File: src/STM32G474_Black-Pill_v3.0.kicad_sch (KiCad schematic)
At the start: 0 parts

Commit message: Add: Schematic to the project. Also added some documents.
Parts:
- added C101, C103, C108, C109, C110, C111, C112, C114, C116, C119, C120: 100nF, symbol Device:C
- added C107: 10µF, symbol Device:C
- added C113, C115, C117, C118: 1µF, symbol Device:C
- added C205, C206, C214, C215: 6pF, Capacitor_SMD:C_0402_1005Metric_Pad0.74x0.62mm_HandSolder, symbol Device:C
- added D101: red, symbol Device:LED
- added D102: BAT54C, Package_TO_SOT_SMD:SOT-23, symbol Diode:BAT54C
- added D103: green, symbol Device:LED
- added J101: USB_C_Receptacle_USB2.0, symbol Connector:USB_C_Receptacle_USB2.0
- added J102, J103: Conn_01x20, symbol Connector_Generic:Conn_01x24
- added J104: Conn_01x04, symbol Connector_Generic:Conn_01x04
- added L101: 10µH, symbol Device:L
- added R101, R102: 5.1k, symbol Device:R
- added R103, R108: 10k, symbol Device:R
- added R104, R105: 10R, symbol Device:R
- added R107, R109: 100R, symbol Device:R
- added R218: 0R, Resistor_SMD:R_0603_1608Metric_Pad0.98x0.95mm_HandSolder, symbol Device:R
- added SW101, SW102, SW103: SW_Push, symbol Switch:SW_Push
- added U101: W25Q32JVSS, Package_SO:SOIC-8_5.23x5.23mm_P1.27mm, symbol Memory_Flash:W25Q32JVSS
- added U102: STM32G474RETx, Package_QFP:LQFP-64_10x10mm_P0.5mm, symbol MCU_ST_STM32G4:STM32G474RETx
- added U103: AP7343xx, Package_TO_SOT_SMD:SOT-23-5, symbol Regulator_Linear_User:AP7343xx
- added Y201: 24MHz, Crystal:Crystal_SMD_SeikoEpson_FA128-4Pin_2.0x1.6mm, symbol Device:Crystal_GND24_Small
- added Y202: 32.768kHz, Crystal:Crystal_SMD_MicroCrystal_CC7V-T1A-2Pin_3.2x1.5mm_HandSoldering, symbol Device:Crystal
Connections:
- new net: J101.A6 (D+), J101.B6 (D+), R105.1
- new net: D103.2 (A), R109.2
- new net: C205.2, U102.5 (PF0), Y201.1
- new net: J101.A5 (CC1), R101.1
- new net: J101.A7 (D-), J101.B7 (D-), R104.1
- new net: J101.B5 (CC2), R102.1
- new net: R218.1, U102.6 (PF1)
- new net: C206.2, R218.2, Y201.3
- new net: D101.2 (A), R107.2
- new net +3.3V: C101.1, C107.1, C108.1, C109.1, C110.1, C111.1, C115.1, C116.1, D102.2, J102.20 (Pin_20), J103.3 (Pin_3), J104.1 (Pin_1), L101.1, R103.1, R107.1, R109.1, SW102.2, U101.3 (IO2), U101.7 (IO3), U101.8 (VCC), U102.16 (VDD), U102.32 (VDD), U102.48 (VDD), U102.64 (VDD), U103.5 (OUT)
- new net +5V: C113.1, C114.1, J101.A4 (VBUS), J101.A9 (VBUS), J101.B4 (VBUS), J101.B9 (VBUS), J102.18 (Pin_18), J103.1 (Pin_1), U103.1 (IN), U103.3 (EN)
- new net BOOT: R108.1, SW102.1, U102.61 (PB8)
- new net GND: C101.2, C103.2, C107.2, C108.2, C109.2, C110.2, C111.2, C112.2, C113.2, C114.2, C115.2, C116.2, C117.1, C118.1, C119.1, C120.1, C205.1, C206.1, C214.1, C215.1, D101.1 (K), J101.A1 (GND), J101.A12 (GND), J101.B1 (GND), J101.B12 (GND), J101.S1 (SHIELD), J102.19 (Pin_19), J102.24 (Pin_24), J103.2 (Pin_2), J103.24 (Pin_24), J104.4 (Pin_4), R101.2, R102.2, R108.2, SW101.1, SW103.1, U101.4 (GND), U102.15 (VSS), U102.27 (VSSA), U102.31 (VSS), U102.47 (VSS), U102.63 (VSS), U103.2 (GND), Y201.2, Y201.4
- new net NRST: C103.1, J103.16 (Pin_16), R103.2, SW101.2, U102.7 (PG10)
- new net PA0: J103.4 (Pin_4), U102.12 (PA0)
- new net PA1: J103.5 (Pin_5), U102.13 (PA1)
- new net PA10: J103.14 (Pin_14), U102.44 (PA10)
- new net PA11: R104.2, U102.45 (PA11)
- new net PA12: R105.2, U102.46 (PA12)
- new net PA15: J103.15 (Pin_15), U101.1 (~{CS}), U102.51 (PA15)
- new net PA2: J103.6 (Pin_6), U102.14 (PA2)
- new net PA3: J103.7 (Pin_7), U102.17 (PA3)
- new net PA4: J103.8 (Pin_8), U102.18 (PA4)
- new net PA5: J103.9 (Pin_9), U102.19 (PA5)
- new net PA6: J103.10 (Pin_10), U102.20 (PA6)
- new net PA7: J103.11 (Pin_11), U102.21 (PA7)
- new net PA8: J103.12 (Pin_12), U102.42 (PA8)
- new net PA9: J103.13 (Pin_13), U102.43 (PA9)
- new net PB0: J102.1 (Pin_1), U102.24 (PB0)
- new net PB1: J102.2 (Pin_2), U102.25 (PB1)
- new net PB10: J102.10 (Pin_10), U102.30 (PB10)
- new net PB11: J102.11 (Pin_11), U102.33 (PB11)
- new net PB12: J102.12 (Pin_12), U102.34 (PB12)
- new net PB13: J102.13 (Pin_13), U102.35 (PB13)
- new net PB14: J102.14 (Pin_14), U102.36 (PB14)
- new net PB15: J102.15 (Pin_15), U102.37 (PB15)
- new net PB2: J102.3 (Pin_3), U102.26 (PB2)
- new net PB3: J102.4 (Pin_4), U102.56 (PB3)
- new net PB4: J102.5 (Pin_5), U102.57 (PB4)
- new net PB5: J102.6 (Pin_6), U102.58 (PB5)
- new net PB6: J102.7 (Pin_7), U102.59 (PB6)
- new net PB7: J102.8 (Pin_8), U102.60 (PB7)
- new net PB9: J102.9 (Pin_9), U102.62 (PB9)
- new net PC0: J103.17 (Pin_17), U102.8 (PC0)
- new net PC1: J103.18 (Pin_18), U102.9 (PC1)
- new net PC13: D103.1 (K), J102.23 (Pin_23), U102.2 (PC13)
- new net PC14: C215.2, U102.3 (PC14), Y202.2
- new net PC15: C214.2, U102.4 (PC15), Y202.1
- new net PC2: J103.19 (Pin_19), U102.10 (PC2)
- new net PC3: J103.21 (Pin_21), U102.11 (PC3)
- new net PC4: J103.22 (Pin_22), U102.22 (PC4)
- new net PC5: J103.23 (Pin_23), U102.23 (PC5)
- new net PC6: J102.16 (Pin_16), U102.38 (PC6)
- new net PC7: J102.17 (Pin_17), U102.39 (PC7)
- new net PC8: J102.21 (Pin_21), U102.40 (PC8)
- new net PC9: J102.22 (Pin_22), U102.41 (PC9)
- new net PD2: SW103.2, U102.55 (PD2)
- new net SPI_{3}.MISO: U101.2 (DO(IO1)), U102.53 (PC11)
- new net SPI_{3}.MOSI: U101.5 (DI(IO0)), U102.54 (PC12)
- new net SPI_{3}.SCK: U101.6 (CLK), U102.52 (PC10)
- new net SWCLK: J104.3 (Pin_3), U102.50 (PA14)
- new net SWDIO: J104.2 (Pin_2), U102.49 (PA13)
- new net VB: D102.1, J103.20 (Pin_20)
- new net VBAT: C112.1, D102.3, U102.1 (VBAT)
- new net VREF: C117.2, C118.2, C119.2, C120.2, L101.2, U102.28 (VREF+), U102.29 (VDDA)
- no-connect marks 0 -> 2
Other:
- note added: "3.3V Power Supply"
- note added: "Analog Voltage Supply / Reference"
- note added: "BOOT Button"
- note added: "Battery Voltage"
- note added: "Decoupling Capacitors (MCU)"
- note added: "Flash"
- note added: "HSE"
- note added: "LSE"
- note added: "Pin-Headers"
- note added: "Power LED"
- note added: "Programming"
- note added: "Reset Button"
- note added: "USB-C"
- note added: "User Button"
- note added: "User LED"
- title: <Default Template> -> Black Pill v3.0 (STM32G474)

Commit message: Mod: Schematic, added manufacturer no. and vendor no.
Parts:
- C101, C108, C109, C110, C111, C112, C114, C116, C119, C120: footprint (none) -> Capacitor_SMD:C_0603_1608Metric
- C104: renamed from C103; footprint (none) -> Capacitor_SMD:C_0603_1608Metric
- C107, C113, C115, C117, C118: footprint (none) -> Capacitor_SMD:C_0603_1608Metric; Manufacturer Part no. (none) -> -; Vendor (none) -> From stock; Vendor Part No. (none) -> -
- C205, C206, C214, C215: footprint Capacitor_SMD:C_0402_1005Metric_Pad0.74x0.62mm_HandSolder -> Capacitor_SMD:C_0402_1005Metric
- D101: footprint (none) -> LED_SMD:LED_0603_1608Metric; Manufacturer Part no. (none) -> LTST-C190KRKT; Vendor (none) -> Digikey; Vendor Part No. (none) -> 160-1436-1-ND
- D102: Manufacturer Part no. (none) -> BAT54C; Vendor (none) -> Digikey; Vendor Part No. (none) -> 4878-BAT54CCT-ND
- D103: footprint (none) -> LED_SMD:LED_0603_1608Metric; Manufacturer Part no. (none) -> LTST-C190KGKT; Vendor (none) -> Digikey; Vendor Part No. (none) -> 160-1435-1-ND
- J101: footprint (none) -> Connector_USB:USB_C_Receptacle_GCT_USB4105-xx-A_16P_TopMnt_Horizontal; Manufacturer Part no. (none) -> USB4105-GF-A; Vendor (none) -> Digikey; Vendor Part No. (none) -> 2073-USB4105-GF-ACT-ND
- J102, J103: footprint (none) -> Connector_PinHeader_2.54mm:PinHeader_1x24_P2.54mm_Vertical; Manufacturer Part no. (none) -> -; Vendor (none) -> From stock; Vendor Part No. (none) -> -
- J104: footprint (none) -> Connector_PinHeader_2.54mm:PinHeader_1x04_P2.54mm_Horizontal; Manufacturer Part no. (none) -> -; Vendor (none) -> From stock; Vendor Part No. (none) -> -
- L101: footprint (none) -> Inductor_SMD:L_0603_1608Metric; Manufacturer Part no. (none) -> MLZ1608M100WT000; Vendor (none) -> Digikey; Vendor Part No. (none) -> 445-6389-1-ND
- R101, R102, R103, R104, R105, R107, R108, R109: footprint (none) -> Resistor_SMD:R_0603_1608Metric; Manufacturer Part no. (none) -> -; Vendor (none) -> From stock; Vendor Part No. (none) -> -
- R218: footprint Resistor_SMD:R_0603_1608Metric_Pad0.98x0.95mm_HandSolder -> Resistor_SMD:R_0603_1608Metric; Vendor BFH-Lager -> From stock
- SW101, SW102, SW103: footprint (none) -> Button_Switch_SMD:SW_SPST_PTS810; Manufacturer Part no. (none) -> PTS810 SJK 250 SMTR LFS; Vendor (none) -> Digikey; Vendor Part No. (none) -> CKN10503CT-ND
- U101: Manufacturer Part no. (none) -> W25Q32JVSSIQ; Vendor (none) -> Digikey; Vendor Part No. (none) -> W25Q32JVSSIQ-ND
- U102: Manufacturer Part no. (none) -> STM32G474RET6; Vendor (none) -> Digikey; Vendor Part No. (none) -> 497-STM32G474RET6-ND
- U103: Manufacturer Part no. (none) -> AP7343-33W5-7; Vendor (none) -> Digikey; Vendor Part No. (none) -> AP7343-33W5-7DICT-ND
- Y202: footprint Crystal:Crystal_SMD_MicroCrystal_CC7V-T1A-2Pin_3.2x1.5mm_HandSoldering -> Crystal:Crystal_SMD_MicroCrystal_CC7V-T1A-2Pin_3.2x1.5mm

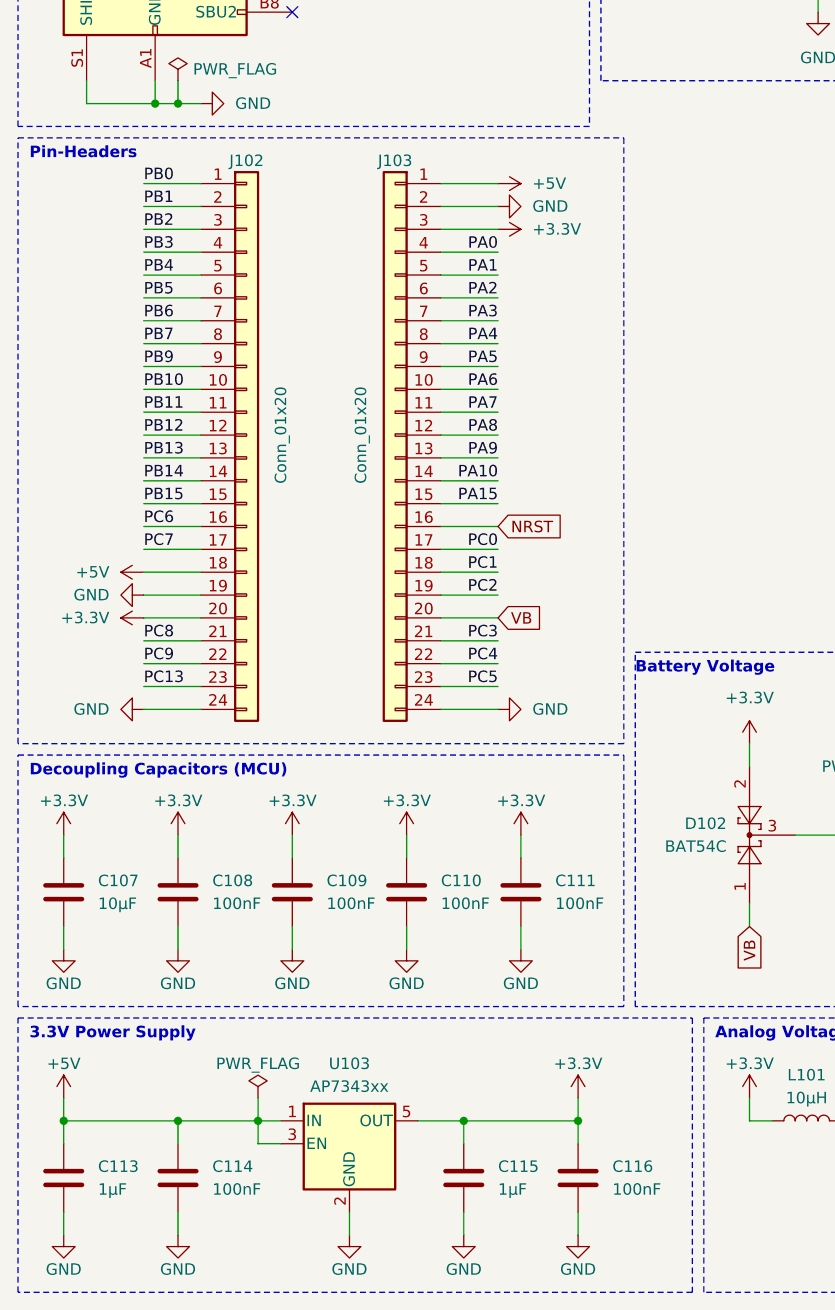
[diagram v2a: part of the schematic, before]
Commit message: Add: PCB Layout and modified schematic to suit the PCB needs
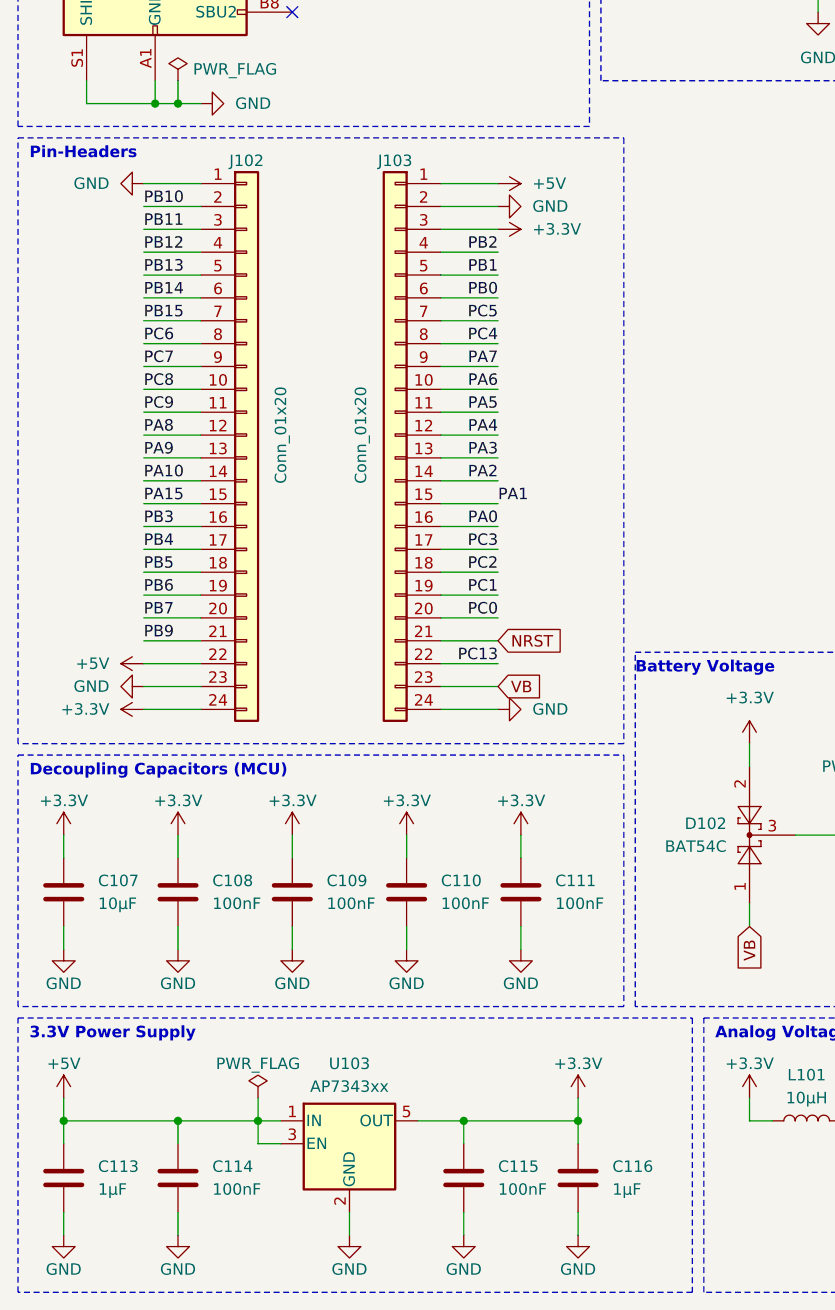
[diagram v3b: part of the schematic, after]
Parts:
- C101, C104, C107, C112, C113, C114, C117, C118, C119, C120: footprint Capacitor_SMD:C_0603_1608Metric -> Capacitor_SMD:C_0402_1005Metric
- C108, C109, C110, C111: footprint Capacitor_SMD:C_0603_1608Metric -> Capacitor_SMD:C_0402_1005Metric; Manufacturer Part no. (none) -> -; Vendor (none) -> From stock; Vendor Part No. (none) -> -
- C115: renamed from C116; footprint Capacitor_SMD:C_0603_1608Metric -> Capacitor_SMD:C_0402_1005Metric
- C116: renamed from C115; footprint Capacitor_SMD:C_0603_1608Metric -> Capacitor_SMD:C_0402_1005Metric
- J104: footprint Connector_PinHeader_2.54mm:PinHeader_1x04_P2.54mm_Horizontal -> Connector_PinHeader_2.54mm_User:PinHeader_1x04_P2.54mm_Horizontal_Board_Edge
- R101, R102, R103, R104, R105, R107, R108, R109, R218: footprint Resistor_SMD:R_0603_1608Metric -> Resistor_SMD:R_0402_1005Metric
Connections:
- net +3.3V: now also J102.24 (Pin_24); no longer J102.20 (Pin_20)
- net +5V: now also J102.22 (Pin_22); no longer J102.18 (Pin_18)
- net GND: now also J102.1 (Pin_1), J102.23 (Pin_23); no longer J102.19 (Pin_19), J102.24 (Pin_24)
- net NRST: now also J103.21 (Pin_21); no longer J103.16 (Pin_16)
- net PA0: now also J103.16 (Pin_16); no longer J103.4 (Pin_4)
- net PA1: now also J103.15 (Pin_15); no longer J103.5 (Pin_5)
- net PA10: now also J102.14 (Pin_14); no longer J103.14 (Pin_14)
- net PA15: now also J102.15 (Pin_15); no longer J103.15 (Pin_15)
- net PA2: now also J103.14 (Pin_14); no longer J103.6 (Pin_6)
- net PA3: now also J103.13 (Pin_13); no longer J103.7 (Pin_7)
- net PA4: now also J103.12 (Pin_12); no longer J103.8 (Pin_8)
- net PA5: now also J103.11 (Pin_11); no longer J103.9 (Pin_9)
- net PA7: now also J103.9 (Pin_9); no longer J103.11 (Pin_11)
- net PA8: now also J102.12 (Pin_12); no longer J103.12 (Pin_12)
- net PA9: now also J102.13 (Pin_13); no longer J103.13 (Pin_13)
- net PB0: now also J103.6 (Pin_6); no longer J102.1 (Pin_1)
- net PB1: now also J103.5 (Pin_5); no longer J102.2 (Pin_2)
- net PB10: now also J102.2 (Pin_2); no longer J102.10 (Pin_10)
- net PB11: now also J102.3 (Pin_3); no longer J102.11 (Pin_11)
- net PB12: now also J102.4 (Pin_4); no longer J102.12 (Pin_12)
- net PB13: now also J102.5 (Pin_5); no longer J102.13 (Pin_13)
- net PB14: now also J102.6 (Pin_6); no longer J102.14 (Pin_14)
- net PB15: now also J102.7 (Pin_7); no longer J102.15 (Pin_15)
- net PB2: now also J103.4 (Pin_4); no longer J102.3 (Pin_3)
- net PB3: now also J102.16 (Pin_16); no longer J102.4 (Pin_4)
- net PB4: now also J102.17 (Pin_17); no longer J102.5 (Pin_5)
- net PB5: now also J102.18 (Pin_18); no longer J102.6 (Pin_6)
- net PB6: now also J102.19 (Pin_19); no longer J102.7 (Pin_7)
- net PB7: now also J102.20 (Pin_20); no longer J102.8 (Pin_8)
- net PB9: now also J102.21 (Pin_21); no longer J102.9 (Pin_9)
- net PC0: now also J103.20 (Pin_20); no longer J103.17 (Pin_17)
- net PC1: now also J103.19 (Pin_19); no longer J103.18 (Pin_18)
- net PC13: now also J103.22 (Pin_22); no longer J102.23 (Pin_23)
- net PC2: now also J103.18 (Pin_18); no longer J103.19 (Pin_19)
- net PC3: now also J103.17 (Pin_17); no longer J103.21 (Pin_21)
- net PC4: now also J103.8 (Pin_8); no longer J103.22 (Pin_22)
- net PC5: now also J103.7 (Pin_7); no longer J103.23 (Pin_23)
- net PC6: now also J102.8 (Pin_8); no longer J102.16 (Pin_16)
- net PC7: now also J102.9 (Pin_9); no longer J102.17 (Pin_17)
- net PC8: now also J102.10 (Pin_10); no longer J102.21 (Pin_21)
- net PC9: now also J102.11 (Pin_11); no longer J102.22 (Pin_22)
- net VB: now also J103.23 (Pin_23); no longer J103.20 (Pin_20)
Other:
- moved on the sheet: C115, C116
